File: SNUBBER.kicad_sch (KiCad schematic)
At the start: 4 parts

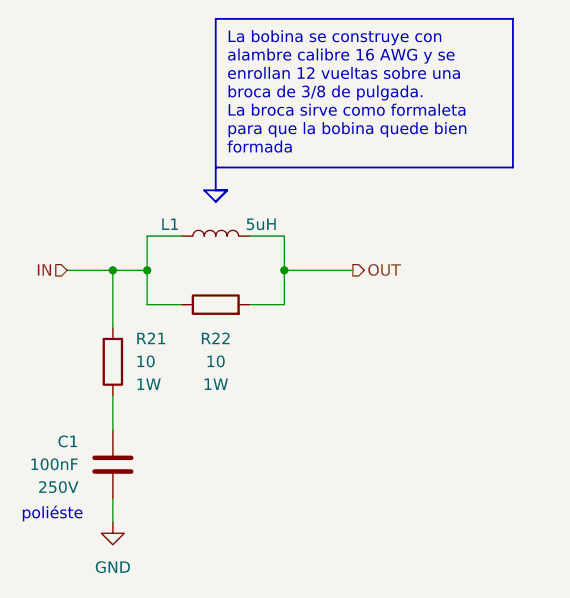
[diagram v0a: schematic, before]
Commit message: mejorando pistas
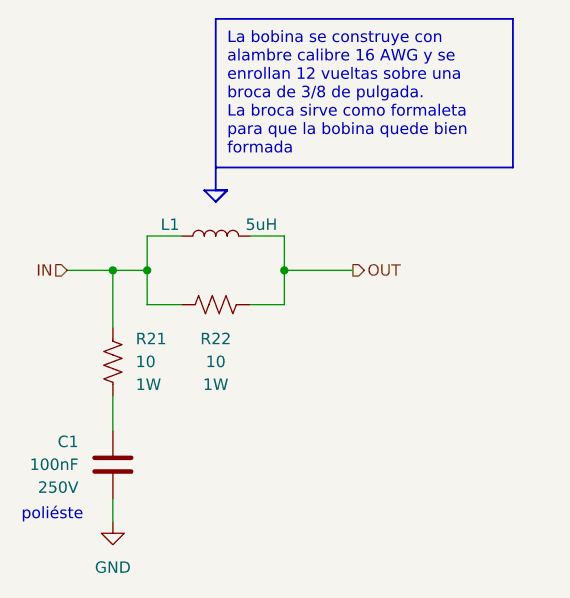
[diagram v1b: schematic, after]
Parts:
- R21, R22: symbol Device:R -> Device:R_US
